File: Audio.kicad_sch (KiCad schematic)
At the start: 15 parts, among them J8 AudioJack3, U10 PCM5121PW, U11 TLV74033PDBVR

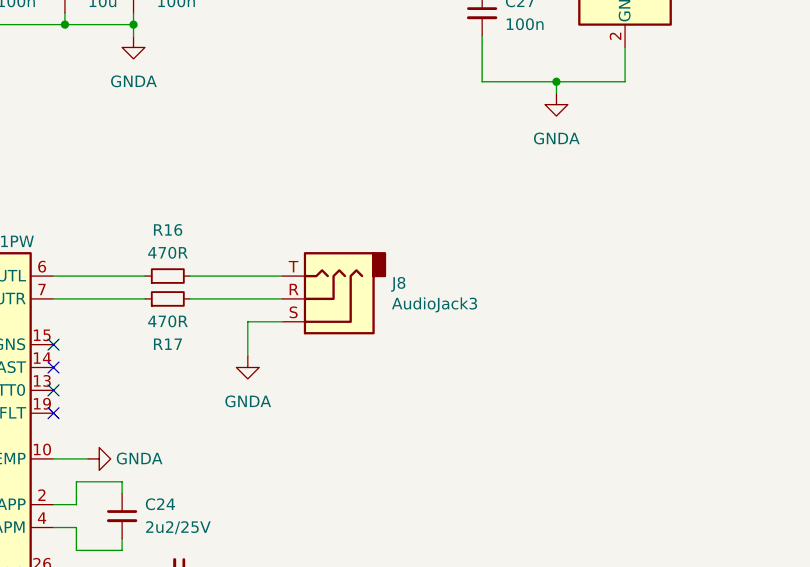
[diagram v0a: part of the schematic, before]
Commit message: Improve SW and D (LED) ordering and silkscreen
Make sure switches (SW) are ordered logically. Also use D1 through D6
for LEDs.

Signed-off-by: Stefan Agner <stefan@agner.ch>
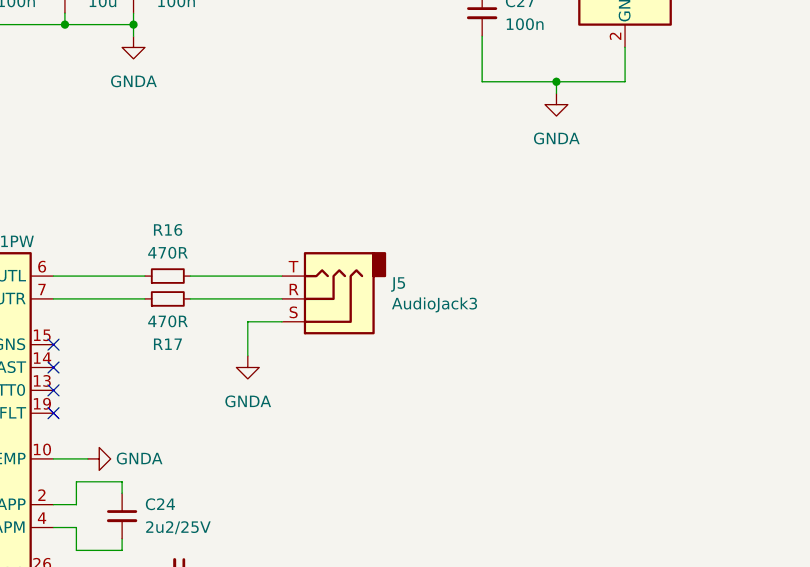
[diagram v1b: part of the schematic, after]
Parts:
- renumbered J8 to J5
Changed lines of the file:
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@@
   (symbol (lib_id "Connector:AudioJack3") (at 158.75 83.185 180) (unit 1)
     (in_bom yes) (on_board yes)
-    (property "Reference" "J8" (id 0) (at 165.8621 81.4514 0)
+    (property "Reference" "J5" (id 0) (at 165.8621 81.4514 0)
       (effects (font (size 1.27 1.27)) (justify right))
     )

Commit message: Fix part number for Audio Jack
Use 3-pin part instead of 4-pin part by defaut (SJ2-35953A-SMT-TR).

Signed-off-by: Stefan Agner <stefan@agner.ch>
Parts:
- J5: PartNumber SJ2-35954A-SMT-TR -> SJ2-35953A-SMT-TR
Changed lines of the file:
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@@
       (effects (font (size 1.27 1.27)) hide)
     )
-    (property "PartNumber" "SJ2-35954A-SMT-TR" (id 5) (at 158.75 83.185 0)
+    (property "PartNumber" "SJ2-35953A-SMT-TR" (id 5) (at 158.75 83.185 0)
       (effects (font (size 1.27 1.27)) hide)
     )

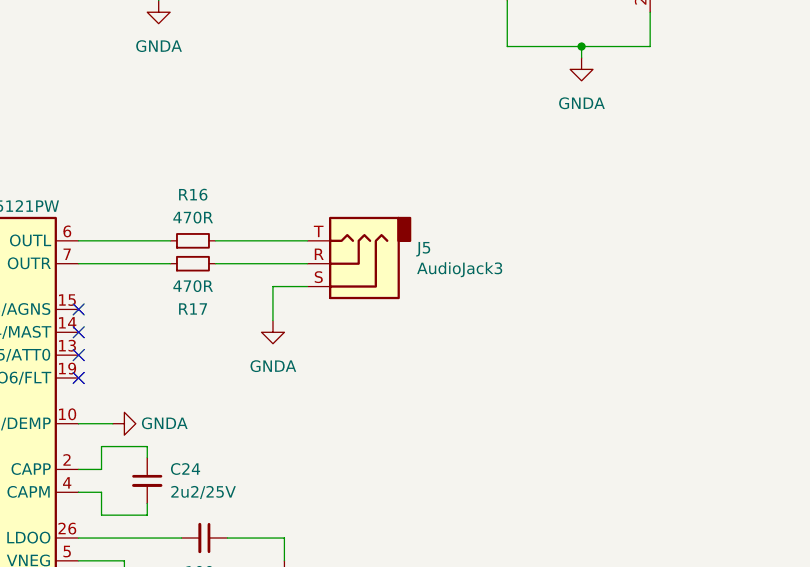
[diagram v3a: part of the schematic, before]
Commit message: Replace CUI SJ2-35953A with through hole HRO PJ-3973-6A
Use a through hole 3.5mm Audio jack to make sure it does nto get teared
off the board accidentially that easily.

Fixes: #9

Signed-off-by: Stefan Agner <stefan@agner.ch>
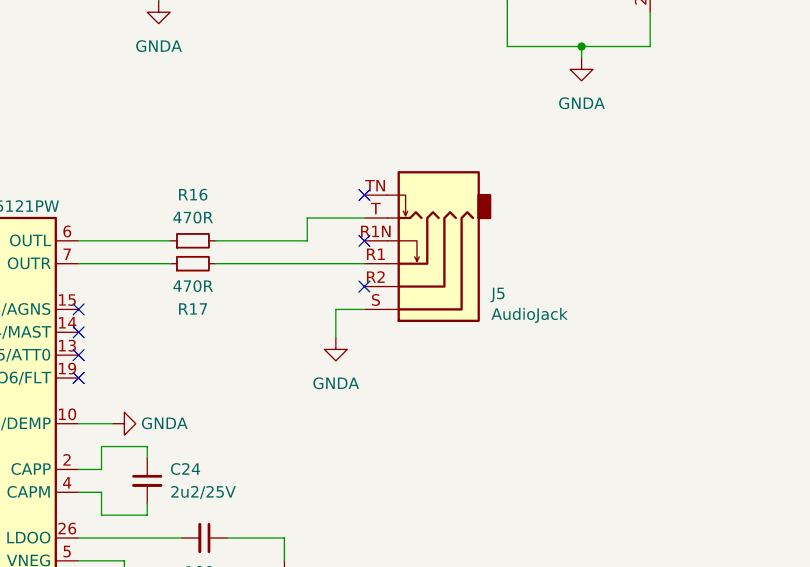
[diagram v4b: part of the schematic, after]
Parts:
- J5: value AudioJack3 -> AudioJack; footprint LightBlue:Jack_3.5mm_CUI_SJ2-35953A-SMT_Horizontal -> LightBlue:Jack_3.5mm_HRO_PJ-3973-6A_Horizontal; symbol Connector:AudioJack3 -> Connector:AudioJack4_SwitchTR1; Manufacturer CUI Devices -> HRO; PartNumber SJ2-35953A-SMT-TR -> PJ-3973-6A
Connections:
- net at R17.2: now also J5.R1; no longer J5.R
- no-connect marks 4 -> 7
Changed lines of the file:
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@@
   (no_connect (at 128.27 93.345))
   (no_connect (at 128.27 95.885))
+  (no_connect (at 160.02 75.565))
+  (no_connect (at 160.02 80.645))
+  (no_connect (at 160.02 85.725))
   (bus_entry (at 82.55 80.645) (size 2.54 2.54)
     (stroke (width 0.1524) (type solid) (color 0 0 0 0))
@@
     (stroke (width 0) (type solid) (color 0 0 0 0))
   )
-  (wire (pts (xy 143.51 83.185) (xy 153.67 83.185))
+  (wire (pts (xy 143.51 83.185) (xy 160.02 83.185))
     (stroke (width 0) (type solid) (color 0 0 0 0))
   )
@@
     (stroke (width 0) (type solid) (color 0 0 0 0))
   )
-  (wire (pts (xy 149.86 85.725) (xy 149.86 89.535))
-    (stroke (width 0) (type solid) (color 0 0 0 0))
-  )
   (wire (pts (xy 151.13 113.665) (xy 151.13 116.205))
     (stroke (width 0) (type solid) (color 0 0 0 0))
   )
-  (wire (pts (xy 153.67 85.725) (xy 149.86 85.725))
+  (wire (pts (xy 153.67 78.105) (xy 160.02 78.105))
+    (stroke (width 0) (type solid) (color 0 0 0 0))
+  )
+  (wire (pts (xy 153.67 80.645) (xy 153.67 78.105))
+    (stroke (width 0) (type solid) (color 0 0 0 0))
+  )
+  (wire (pts (xy 156.845 88.265) (xy 160.02 88.265))
+    (stroke (width 0) (type solid) (color 0 0 0 0))
+  )
+  (wire (pts (xy 156.845 91.44) (xy 156.845 88.265))
     (stroke (width 0) (type solid) (color 0 0 0 0))
   )
@@
     (pin "1")
   )
-  (symbol (lib_id "power:GNDA") (at 149.86 89.535 0) (unit 1)
-    (in_bom yes) (on_board yes)
-    (property "Reference" "#PWR0167" (id 0) (at 149.86 95.885 0)
-      (effects (font (size 1.27 1.27)) hide)
-    )
-    (property "Value" "GNDA" (id 1) (at 149.86 94.615 0))
-    (property "Footprint" "" (id 2) (at 149.86 89.535 0)
-      (effects (font (size 1.27 1.27)) hide)
-    )
-    (property "Datasheet" "" (id 3) (at 149.86 89.535 0)
-      (effects (font (size 1.27 1.27)) hide)
-    )
-    (pin "1")
-  )
   (symbol (lib_id "power:GNDA") (at 151.13 116.205 0) (unit 1)
     (in_bom yes) (on_board yes)
@@
     )
     (property "Datasheet" "" (id 3) (at 151.13 116.205 0)
+      (effects (font (size 1.27 1.27)) hide)
+    )
+    (pin "1")
+  )
+  (symbol (lib_id "power:GNDA") (at 156.845 91.44 0) (unit 1)
+    (in_bom yes) (on_board yes)
+    (property "Reference" "#PWR0167" (id 0) (at 156.845 97.79 0)
+      (effects (font (size 1.27 1.27)) hide)
+    )
+    (property "Value" "GNDA" (id 1) (at 156.845 96.52 0))
+    (property "Footprint" "" (id 2) (at 156.845 91.44 0)
+      (effects (font (size 1.27 1.27)) hide)
+    )
+    (property "Datasheet" "" (id 3) (at 156.845 91.44 0)
       (effects (font (size 1.27 1.27)) hide)
     )
@@
     (pin "2")
   )
-  (symbol (lib_id "Connector:AudioJack3") (at 158.75 83.185 180) (unit 1)
-    (in_bom yes) (on_board yes)
-    (property "Reference" "J5" (id 0) (at 165.8621 81.4514 0)
-      (effects (font (size 1.27 1.27)) (justify right))
-    )
-    (property "Value" "AudioJack3" (id 1) (at 165.8621 83.7501 0)
-      (effects (font (size 1.27 1.27)) (justify right))
-    )
-    (property "Footprint" "LightBlue:Jack_3.5mm_CUI_SJ2-35953A-SMT_Horizontal" (id 2) (at 158.75 83.185 0)
-      (effects (font (size 1.27 1.27)) hide)
-    )
-    (property "Datasheet" "~" (id 3) (at 158.75 83.185 0)
-      (effects (font (size 1.27 1.27)) hide)
-    )
-    (property "Manufacturer" "CUI Devices" (id 4) (at 158.75 83.185 0)
-      (effects (font (size 1.27 1.27)) hide)
-    )
-    (property "PartNumber" "SJ2-35953A-SMT-TR" (id 5) (at 158.75 83.185 0)
-      (effects (font (size 1.27 1.27)) hide)
-    )
-    (property "Config" "+Audio" (id 6) (at 158.75 83.185 0)
-      (effects (font (size 1.27 1.27)) hide)
-    )
-    (pin "R")
-    (pin "S")
-    (pin "T")
-  )
   (symbol (lib_id "Regulator_Linear:TLV73333PDBV") (at 191.77 47.625 0) (unit 1)
     (in_bom yes) (on_board yes)
@@
       (effects (font (size 1.27 1.27)) hide)
     )
-    (property "Config" "+Audio" (id 4) (at 191.77 47.625 0)
+    (property "Config" "+Audio" (id 6) (at 191.77 47.625 0)
       (effects (font (size 1.27 1.27)) hide)
     )
@@
     (pin "5")
   )
+  (symbol (lib_id "Connector:AudioJack4_SwitchTR1") (at 165.1 83.185 180) (unit 1)
+    (in_bom yes) (on_board yes)
+    (property "Reference" "J5" (id 0) (at 174.1171 86.5314 0)
+      (effects (font (size 1.27 1.27)) (justify right))
+    )
+    (property "Value" "AudioJack" (id 1) (at 174.117 88.83 0)
+      (effects (font (size 1.27 1.27)) (justify right))
+    )
+    (property "Footprint" "LightBlue:Jack_3.5mm_HRO_PJ-3973-6A_Horizontal" (id 2) (at 166.37 83.185 0)
+      (effects (font (size 1.27 1.27)) hide)
+    )
+    (property "Datasheet" "https://datasheet.lcsc.com/szlcsc/2009061735_Korean-Hroparts-Elec-PJ-3973-6A_C707261.pdf" (id 3) (at 166.37 83.185 0)
+      (effects (font (size 1.27 1.27)) hide)
+    )
+    (property "Manufacturer" "HRO" (id 4) (at 165.1 83.185 0)
+      (effects (font (size 1.27 1.27)) hide)
+    )
+    (property "PartNumber" "PJ-3973-6A" (id 5) (at 165.1 83.185 0)
+      (effects (font (size 1.27 1.27)) hide)
+    )
+    (property "Config" "+Audio" (id 6) (at 165.1 83.185 0)
+      (effects (font (size 1.27 1.27)) hide)
+    )
+    (pin "R1")
+    (pin "R1N")
+    (pin "R2")
+    (pin "S")
+    (pin "T")
+    (pin "TN")
+  )
   (symbol (lib_id "Audio:PCM5121PW") (at 110.49 98.425 0) (unit 1)

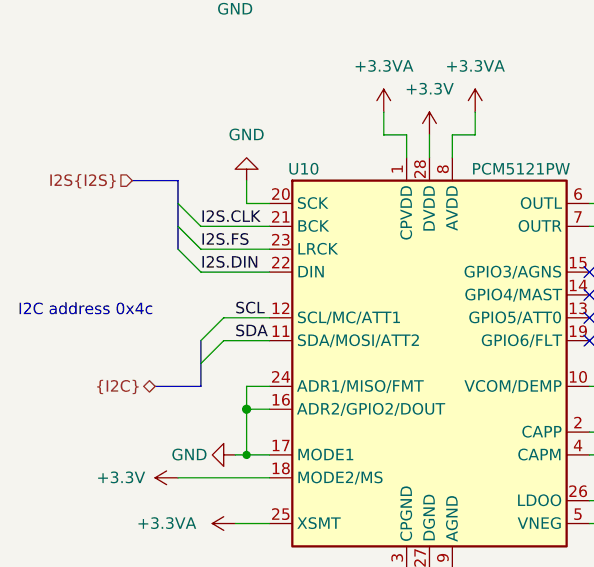
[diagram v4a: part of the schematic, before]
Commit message: Assign footprints and annotate components
Signed-off-by: Stefan Agner <stefan@agner.ch>
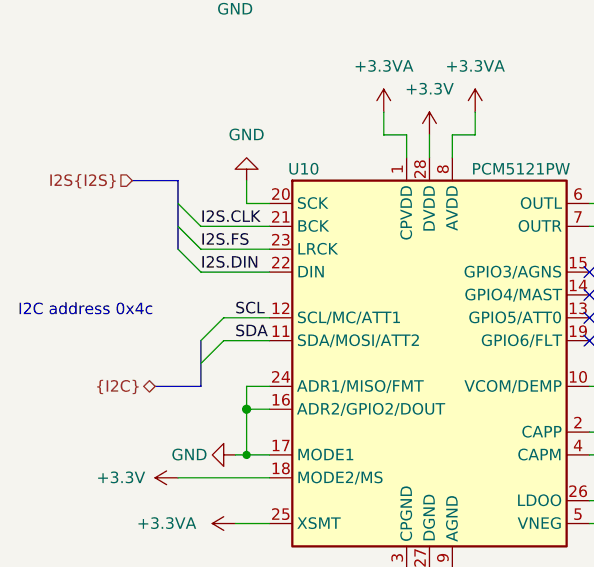
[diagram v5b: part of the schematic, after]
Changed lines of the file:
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@@
-(kicad_sch (version 20210126) (generator eeschema)
+(kicad_sch (version 20210406) (generator eeschema)
   (paper "A4")
   (title_block
@@
     (stroke (width 0) (type solid) (color 0 0 0 0))
   )
-  (bus (pts (xy 82.55 78.105) (xy 82.55 80.645))
-    (stroke (width 0) (type solid) (color 0 0 0 0))
-  )
-  (bus (pts (xy 82.55 80.645) (xy 82.55 83.185))
-    (stroke (width 0) (type solid) (color 0 0 0 0))
-  )
-  (bus (pts (xy 82.55 83.185) (xy 82.55 85.725))
-    (stroke (width 0) (type solid) (color 0 0 0 0))
-  )
-  (bus (pts (xy 85.09 95.885) (xy 85.09 98.425))
-    (stroke (width 0) (type solid) (color 0 0 0 0))
-  )
-  (bus (pts (xy 85.09 98.425) (xy 85.09 100.965))
-    (stroke (width 0) (type solid) (color 0 0 0 0))
-  )
+  (bus (pts (xy 82.55 78.105) (xy 82.55 85.725))
+    (stroke (width 0) (type solid) (color 0 0 0 0))
+  )
+  (bus (pts (xy 85.09 95.885) (xy 85.09 100.965))
+    (stroke (width 0) (type solid) (color 0 0 0 0))
+  )

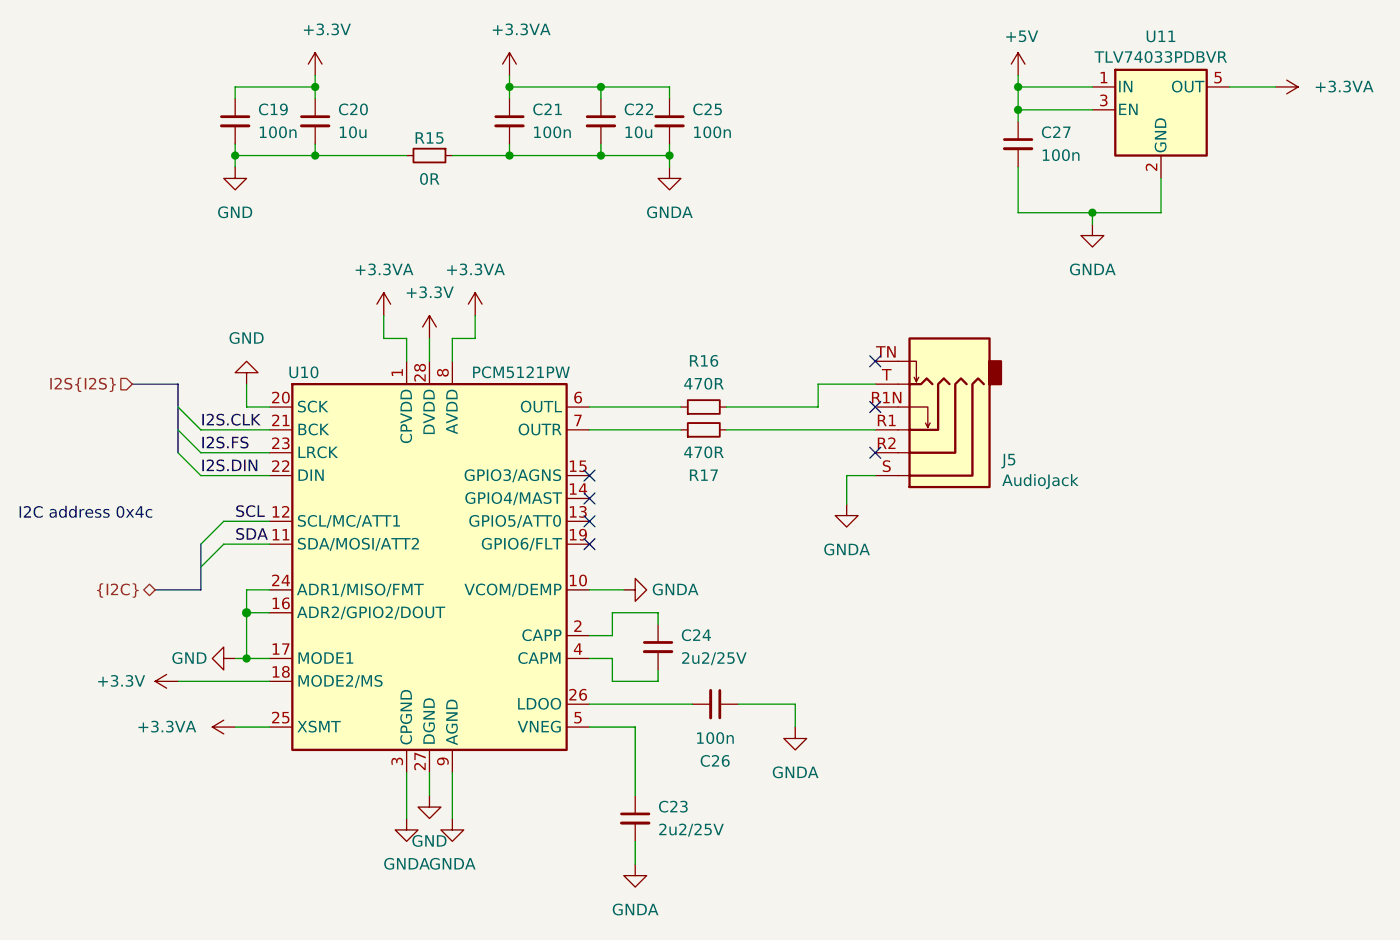
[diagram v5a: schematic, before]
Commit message: Reannotate the complete schematics
Signed-off-by: Stefan Agner <stefan@agner.ch>
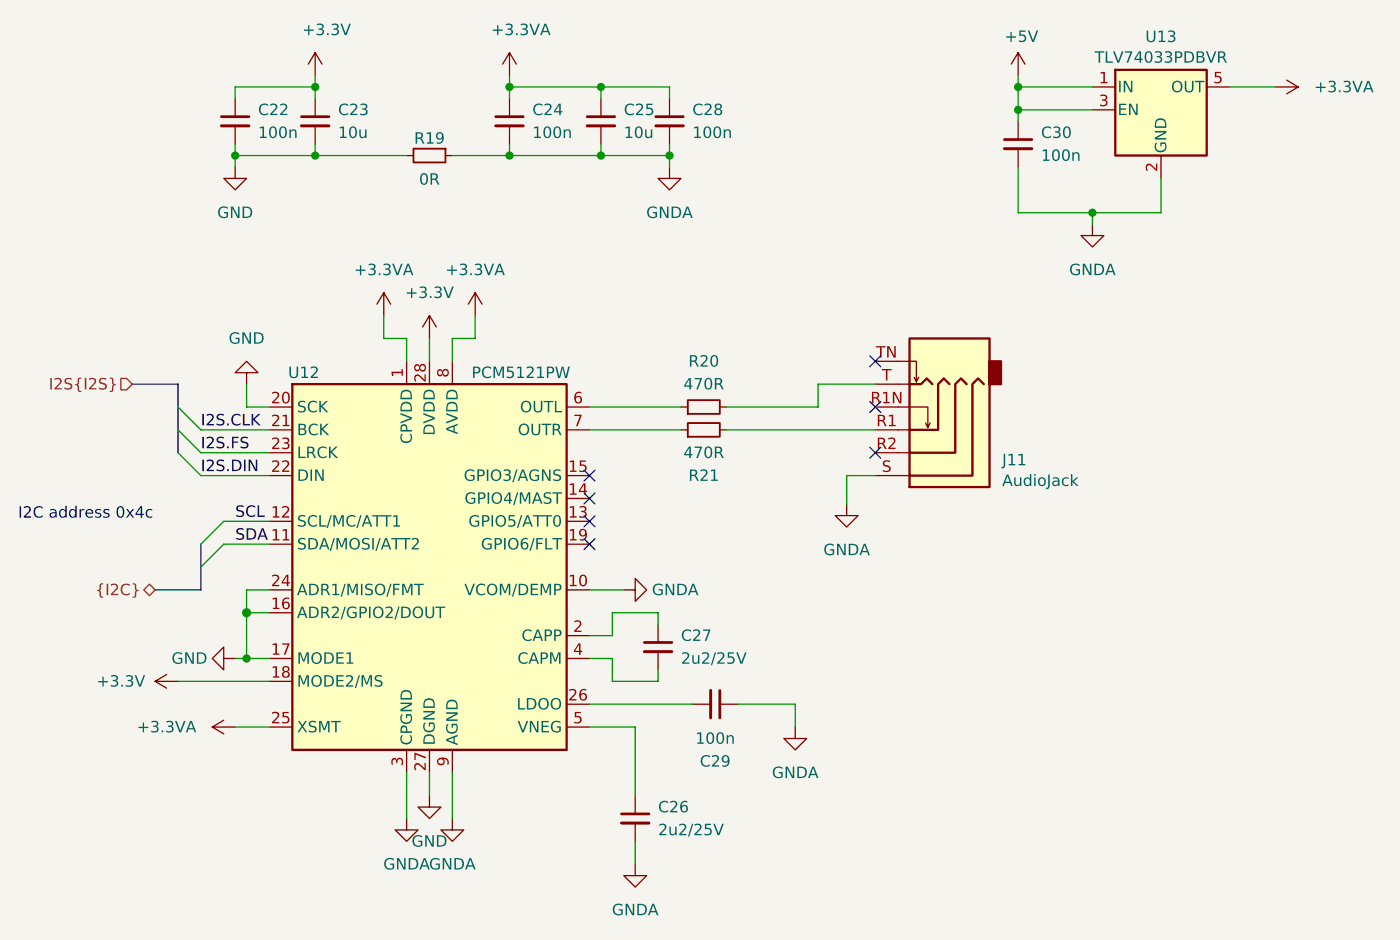
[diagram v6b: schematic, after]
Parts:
- renumbered C19 to C22, C20 to C23, C21 to C24, C22 to C25, C23 to C26, C24 to C27, C25 to C28, C26 to C29, C27 to C30, J5 to J11, R15 to R19, R16 to R20, R17 to R21, U10 to U12, U11 to U13

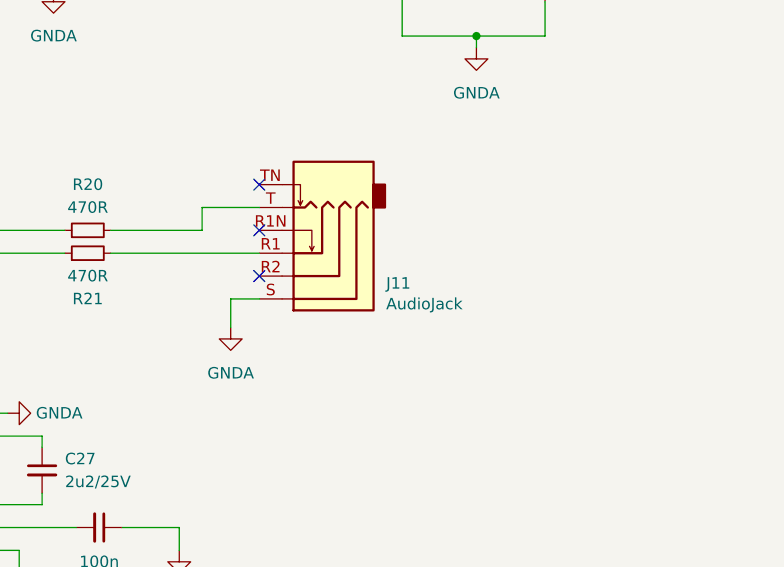
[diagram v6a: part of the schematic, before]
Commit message: Adjust rating/footprint size of some ceramic capacitors
Also update connector/jumper designator to make more sense.

Signed-off-by: Stefan Agner <stefan@agner.ch>
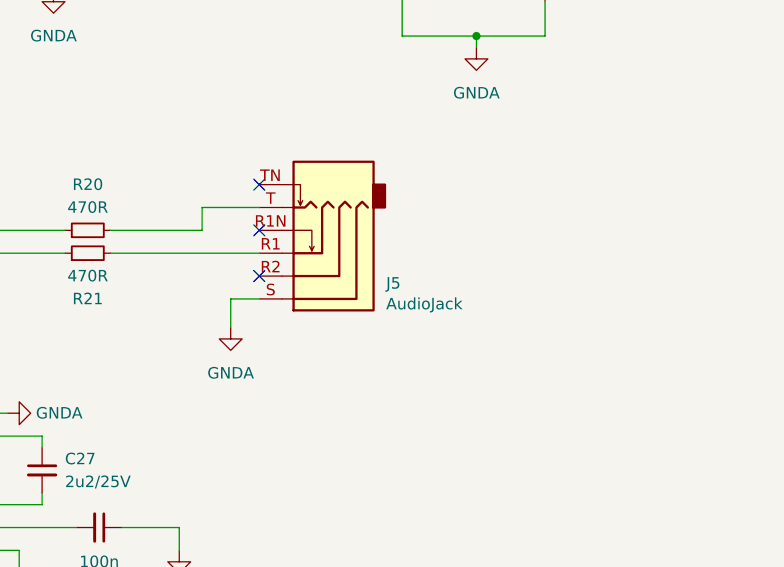
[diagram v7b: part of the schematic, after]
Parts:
- renumbered J11 to J5
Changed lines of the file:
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@@
   (symbol (lib_id "Connector:AudioJack4_SwitchTR1") (at 165.1 83.185 180) (unit 1)
     (in_bom yes) (on_board yes)
-    (property "Reference" "J11" (id 0) (at 174.1171 86.5314 0)
+    (property "Reference" "J5" (id 0) (at 174.1171 86.5314 0)
       (effects (font (size 1.27 1.27)) (justify right))
     )

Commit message: Use 0805 package for Audio 2.2uF/25V capacitors
Fixes: #20

Signed-off-by: Stefan Agner <stefan@agner.ch>
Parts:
- C26, C27: footprint Capacitor_SMD:C_0402_1005Metric -> Capacitor_SMD:C_0805_2012Metric
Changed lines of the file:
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@@
       (effects (font (size 1.27 1.27)) (justify right))
     )
-    (property "Footprint" "Capacitor_SMD:C_0402_1005Metric" (id 2) (at 133.35 126.365 0)
+    (property "Footprint" "Capacitor_SMD:C_0805_2012Metric" (id 2) (at 133.35 126.365 0)
       (effects (font (size 1.27 1.27)) hide)
     )
@@
       (effects (font (size 1.27 1.27)) (justify left))
     )
-    (property "Footprint" "Capacitor_SMD:C_0402_1005Metric" (id 2) (at 135.89 107.315 0)
+    (property "Footprint" "Capacitor_SMD:C_0805_2012Metric" (id 2) (at 135.89 107.315 0)
       (effects (font (size 1.27 1.27)) hide)
     )
